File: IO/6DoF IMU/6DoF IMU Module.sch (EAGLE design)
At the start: 18 parts, among them U1 MPU-6050

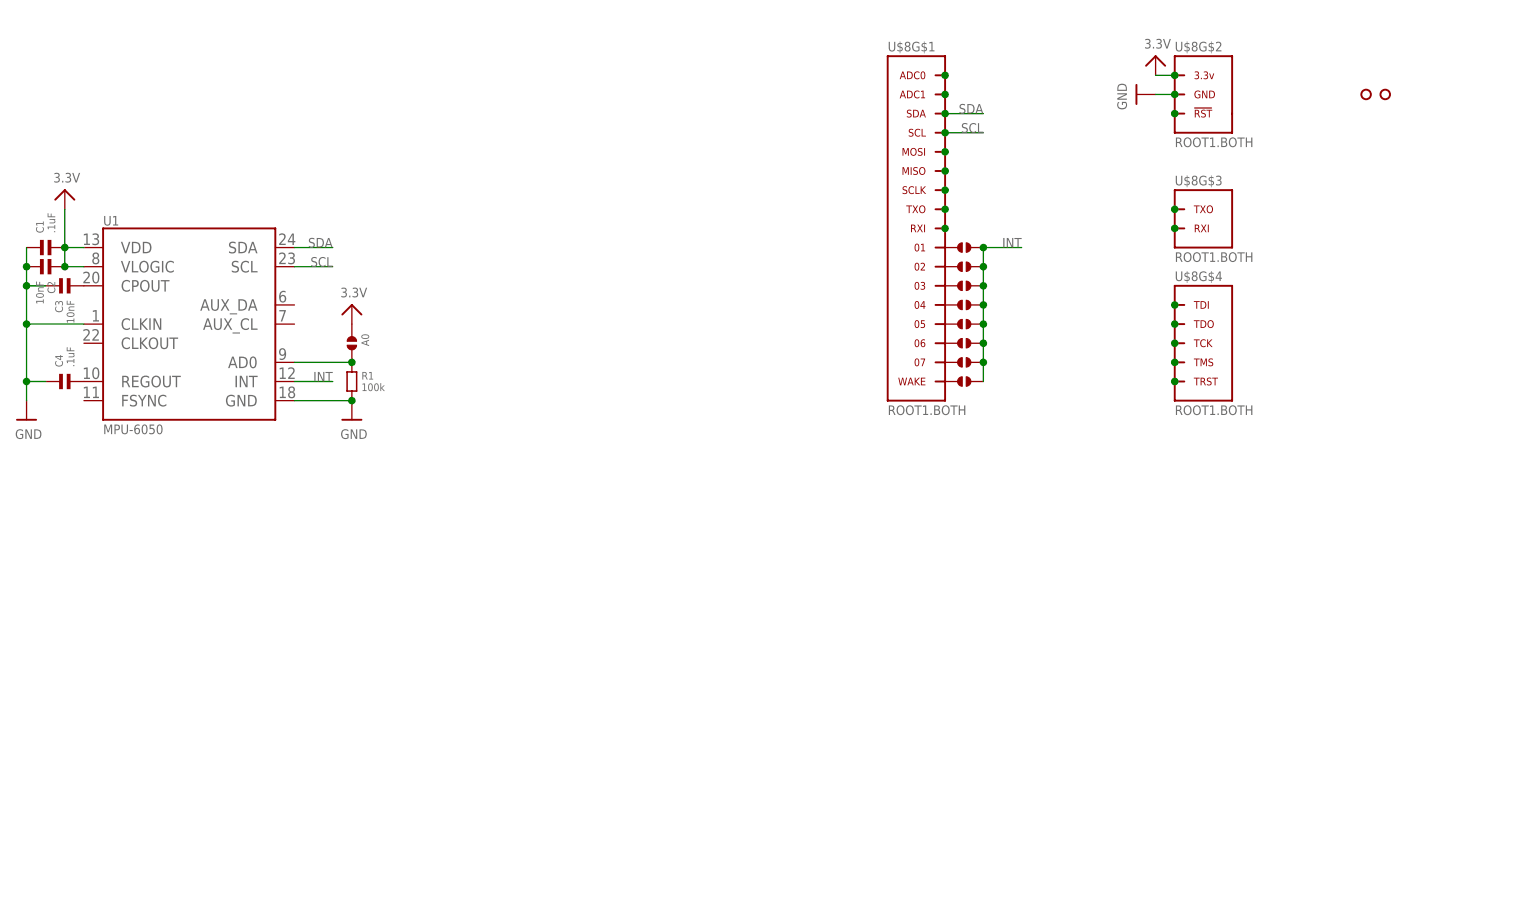
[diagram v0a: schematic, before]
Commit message: Updated 6DoF IMU Module silkscreen and connections.
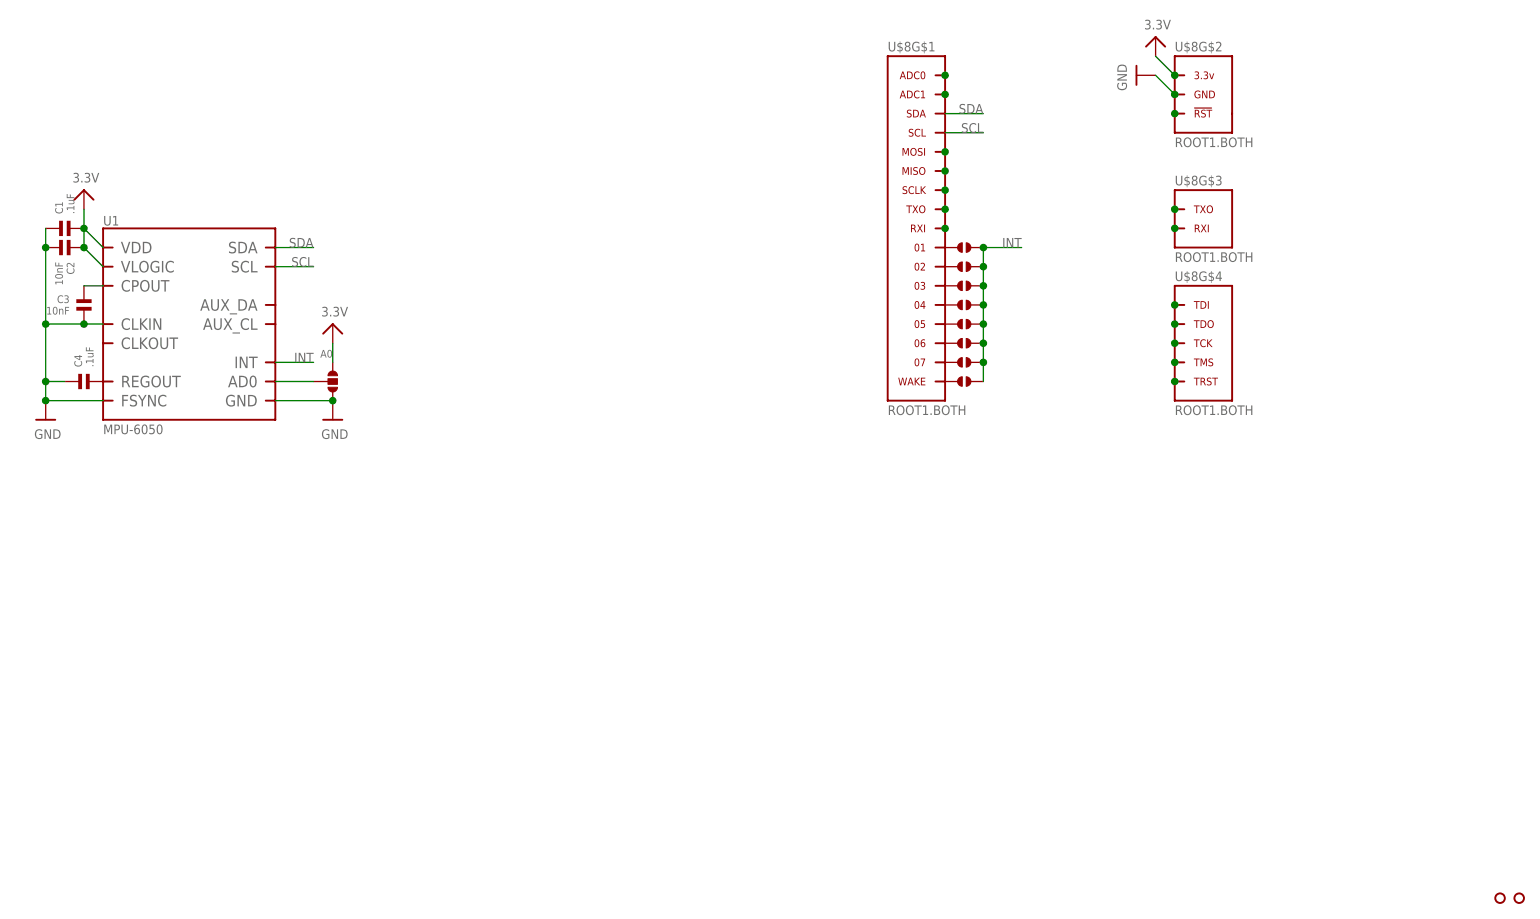
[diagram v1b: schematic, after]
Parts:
- removed R1: 100k, .standardparts:RESISTOR.0603
- removed U$3: HOLE.2MM, .screw_holes:HOLE.2MM
- added U$12: HOLE.#2, .screw_holes:HOLE.#2
- A0: device .solderjumper:SOLDERJUMPER.2.LRG -> .solderjumper:SOLDERJUMPER.3.MED.23
- U$4: value HOLE.2MM -> HOLE.#2; device .screw_holes:HOLE.2MM -> .screw_holes:HOLE.#2
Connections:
- removed net N$16: C3.2, U1.CPOUT
- new net N$27: C3.1, U1.CPOUT
- net GND: now also A0.3, C3.2, U1.FSYNC; no longer C3.1, R1.2
- net N$18: no longer R1.1
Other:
- moved on the sheet: C1, C2, C3, C4
